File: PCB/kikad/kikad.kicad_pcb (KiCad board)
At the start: 2 copper layers, 228.6 x 137.2 mm, 603 parts, among them M1 SSOP-24_5.3x8.2mm_P0.65mm, M2 SSOP-24_5.3x8.2mm_P0.65mm, m1 PinHeader_1x02_P1.00mm_Vertic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, m2 PinHeader_1x02_P1.00mm_Vertic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, m3 PinHeader_1x02_P1.00mm_Vertic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, m4 PinHeader_1x02_P1.00mm_Vertic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

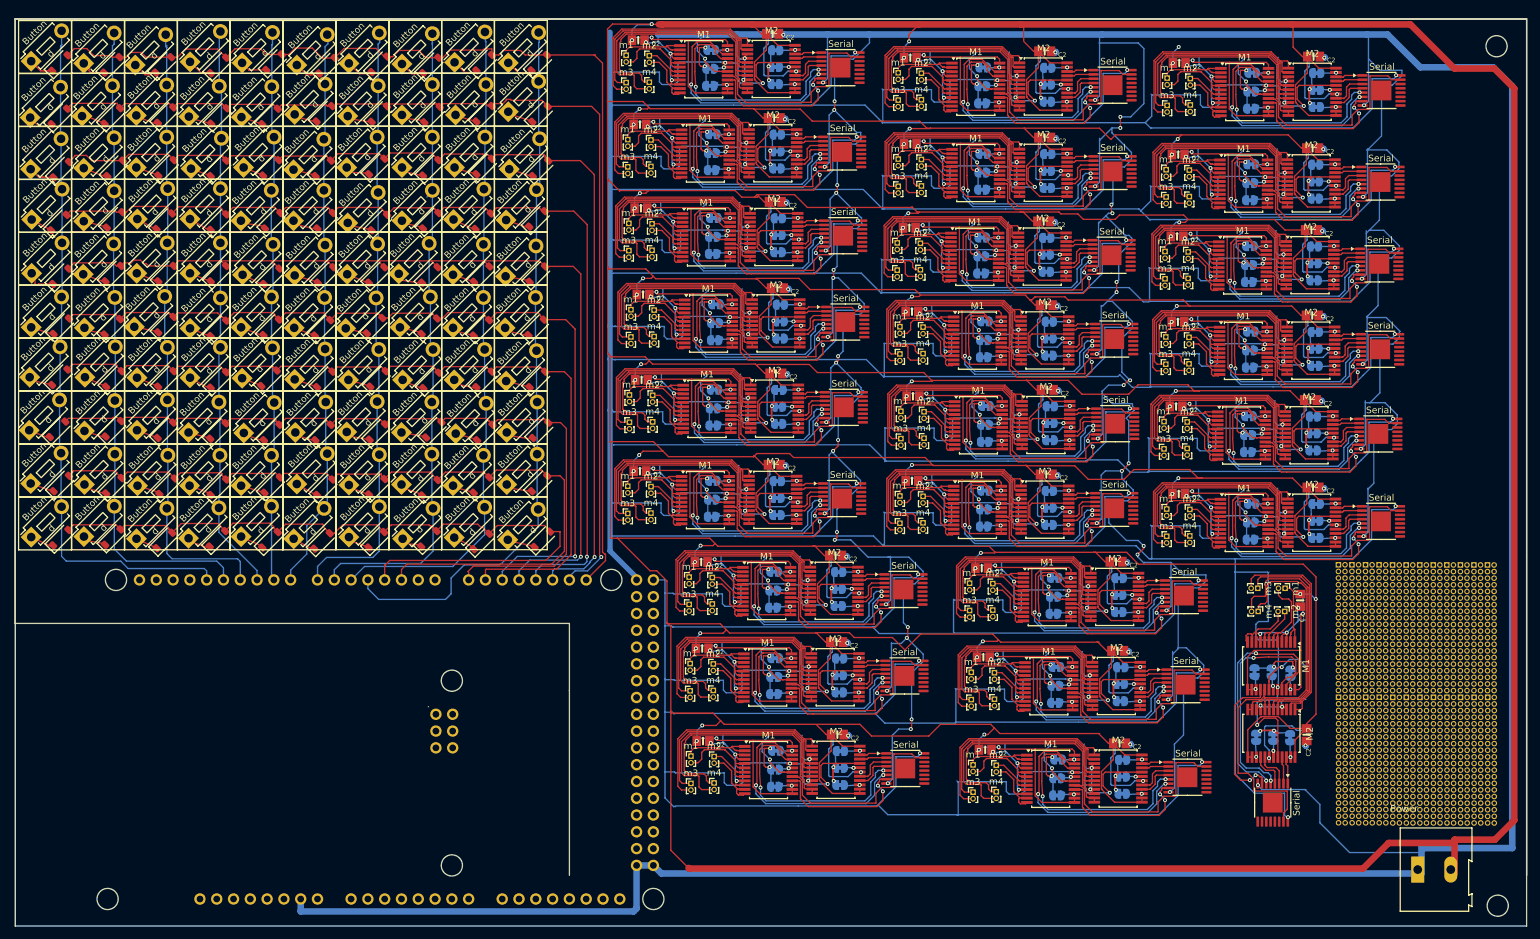
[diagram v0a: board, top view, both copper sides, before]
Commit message: kicad motors all connected up
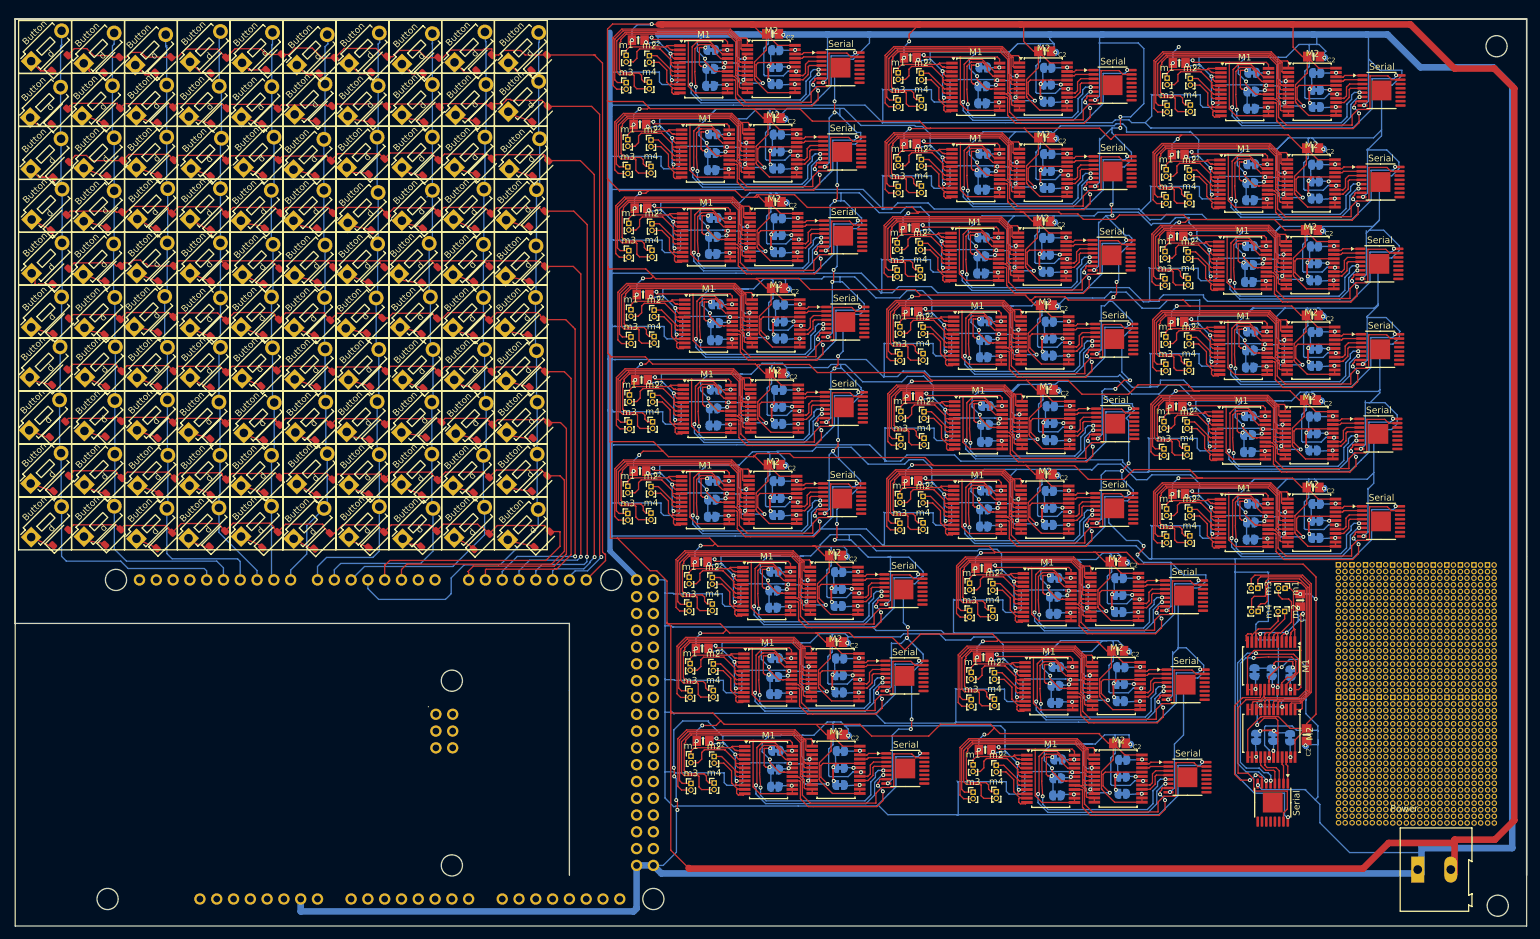
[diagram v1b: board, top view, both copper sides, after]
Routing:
- net (no net): track 18679.6 -> 19709.1 mm, vias 808 -> 812

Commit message: pcvb
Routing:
- net (no net): track 19709.1 -> 19995.4 mm, vias 812 -> 842
